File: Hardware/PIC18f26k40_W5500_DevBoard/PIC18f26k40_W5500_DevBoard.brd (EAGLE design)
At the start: 58.1 x 66.1 mm, 61 parts, among them J2 MAGJACK, J6 USB-B, U1 W5500, U2 PIC18F2523-I/SO, Y2 CRYSTAL-GROUNDEDSMD-3.2X2.5

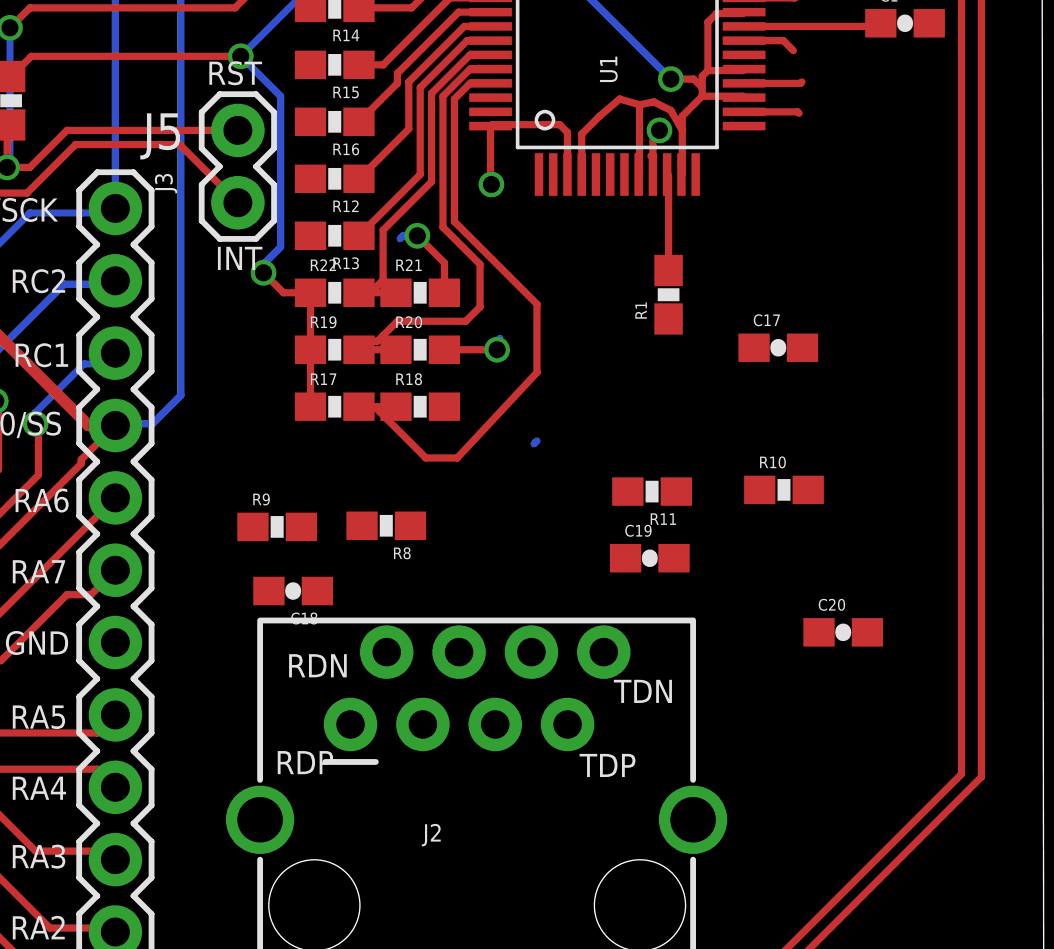
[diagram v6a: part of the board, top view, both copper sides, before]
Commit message: #302 Finished Routing Wiznet Dev Board
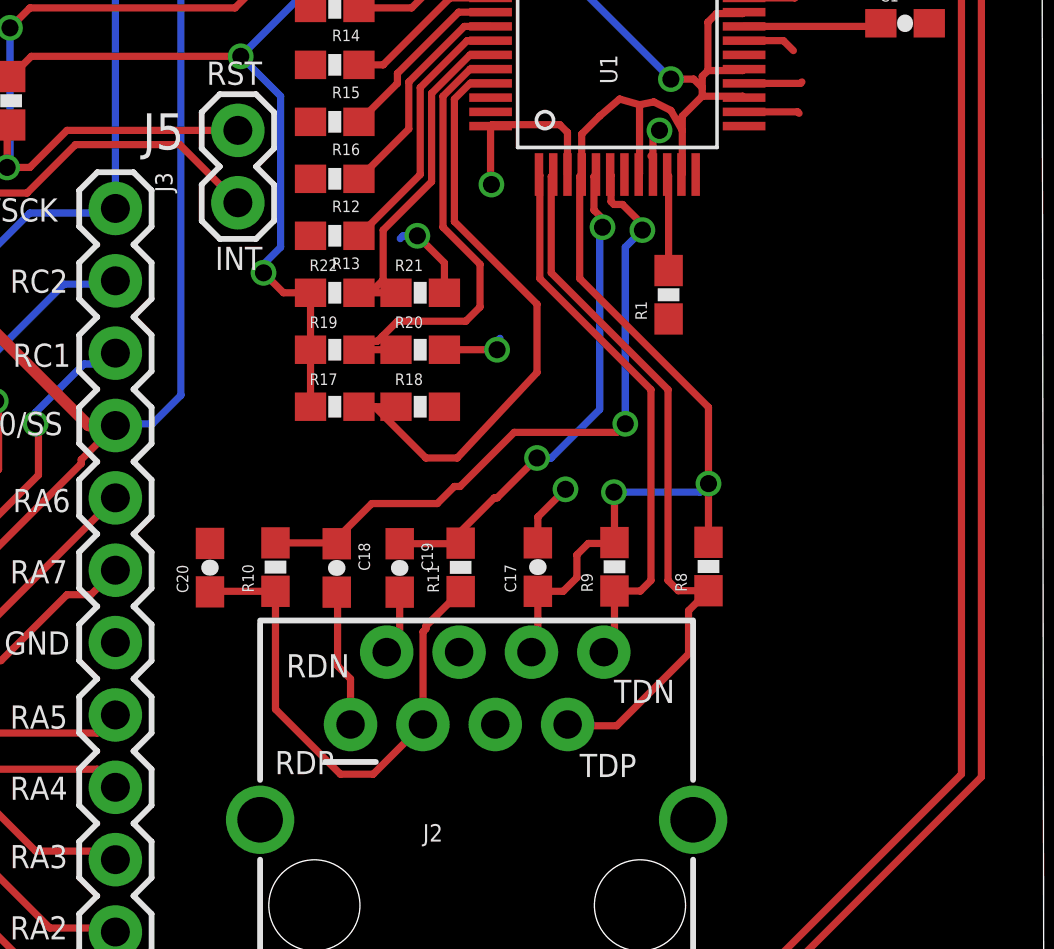
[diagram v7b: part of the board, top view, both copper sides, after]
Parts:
- moved C20 22.3 mm to (28.7, 22.9), turned to 90 degrees
- moved R10 18.1 mm to (31.0, 23.0), turned to 90 degrees
- moved R9 11.9 mm to (42.9, 23.0), turned to 90 degrees
- moved C17 11.4 mm to (40.2, 23.0), turned to 90 degrees
- moved R8 11.4 mm to (46.2, 23.0), turned to 90 degrees
- moved C19 8.79 mm to (35.4, 22.9), turned to 270 degrees
- moved R11 7.23 mm to (37.5, 23.0), turned to 90 degrees
- moved C18 1.73 mm to (33.2, 22.9), turned to 270 degrees
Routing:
- net VCCA: track 65.9 -> 92.0 mm, vias 2 -> 4
- net TDP: track 0.00 -> 25.4 mm
- net RDP: track 0.00 -> 23.8 mm, vias 0 -> 2
- net TDN: track 0.00 -> 19.6 mm
- net N$11: track 0.00 -> 18.5 mm
- net RDN: track 0.00 -> 17.7 mm, vias 0 -> 2
- net N$8: track 0.00 -> 4.85 mm
- net N$10: track 0.00 -> 2.29 mm
- net GND: track 28.7 -> 30.8 mm, vias 7 -> 8

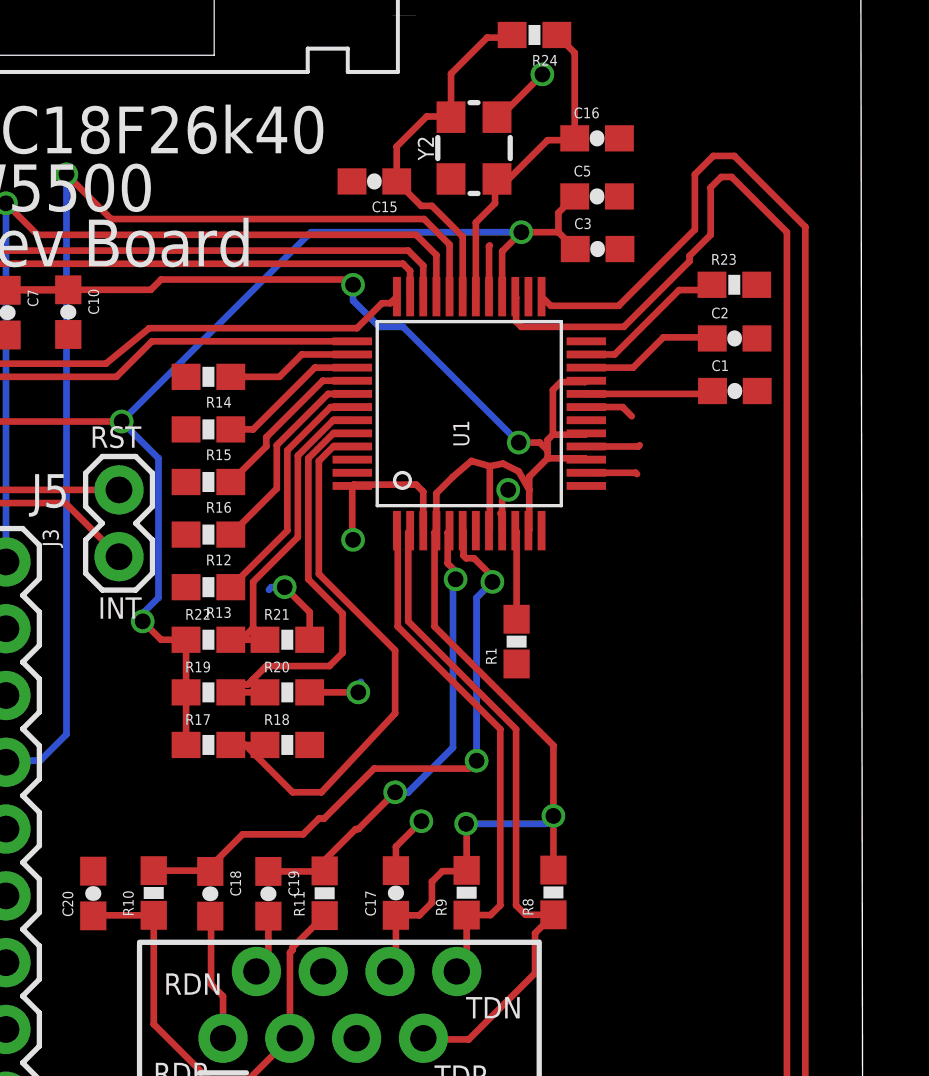
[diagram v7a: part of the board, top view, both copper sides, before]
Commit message: #302 DRC passing on PIC W5500 Board
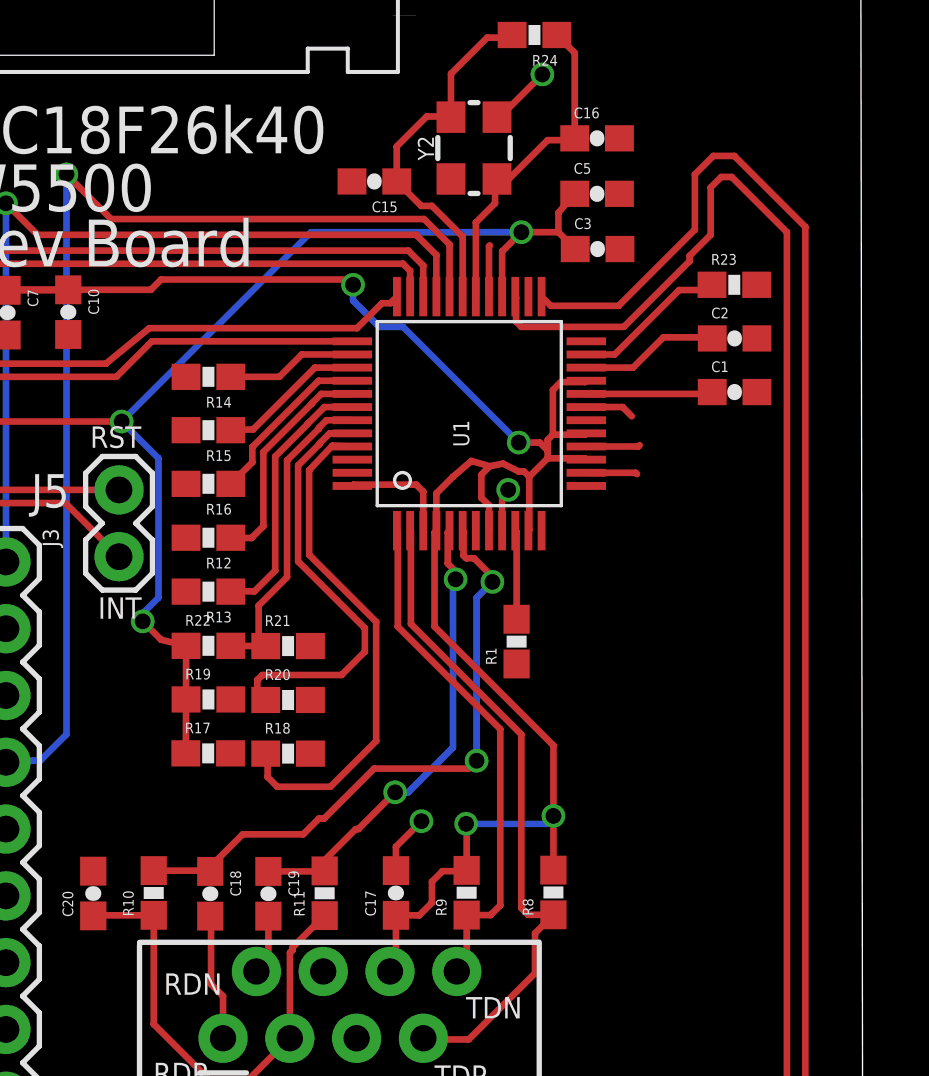
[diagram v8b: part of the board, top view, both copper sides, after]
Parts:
- moved R18 0.33 mm to (36.1, 28.3)
- moved R17 0.32 mm to (33.1, 28.3)
- moved R20 0.29 mm to (36.1, 30.3)
- moved R19 0.27 mm to (33.1, 30.3)
- moved R21 0.24 mm to (36.1, 32.4)
- moved R22 0.23 mm to (33.1, 32.4)
- moved R13 0.17 mm to (33.1, 34.4)
- moved R12 0.12 mm to (33.1, 36.5)
- moved C5 0.10 mm to (47.9, 49.6)
- moved R16 0.07 mm to (33.1, 38.5)
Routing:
- net GND: track 30.8 -> 23.3 mm, vias 8 -> 5
- net PMODE0: track 21.3 -> 19.3 mm
- net N$15: track 9.24 -> 10.1 mm
- net PMODE2: track 12.9 -> 12.1 mm
- net N$3: track 7.80 -> 8.55 mm
- net PMODE1: track 16.8 -> 16.1 mm
